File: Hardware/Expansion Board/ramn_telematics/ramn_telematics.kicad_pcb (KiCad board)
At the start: 2 copper layers, 63.3 x 33.3 mm, 43 parts, among them IC1 ESP32-S3-WROOM-1-N8, IC2 SGM2212-3.3XKC3G_TR, J1 Main RAMN Connection, J2 105164-0001, J4 105164-0001, Q1 L8050QLT1G, Q2 L8050QLT1G, U1 CP2102N-Axx-xQFN28

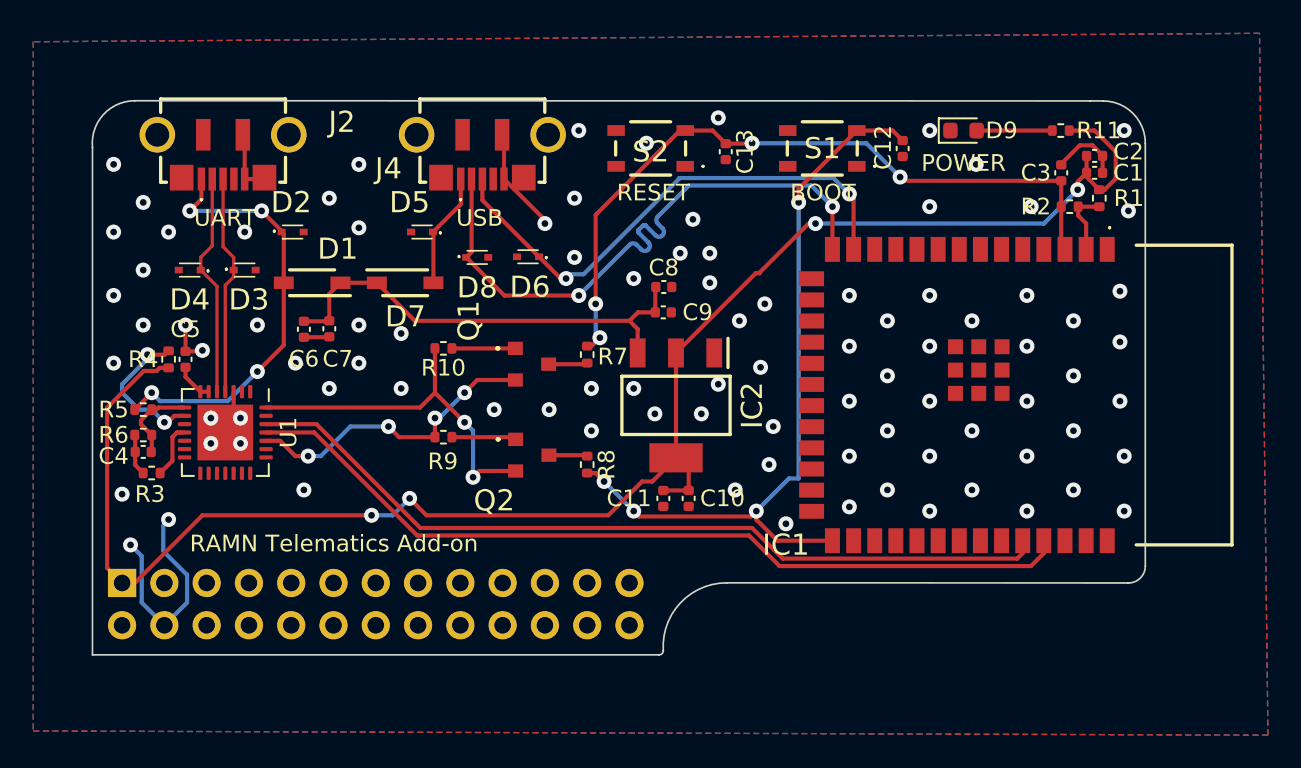
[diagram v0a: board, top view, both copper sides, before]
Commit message: More Board Revisions
Trying to update to components that are available in JLCPCB
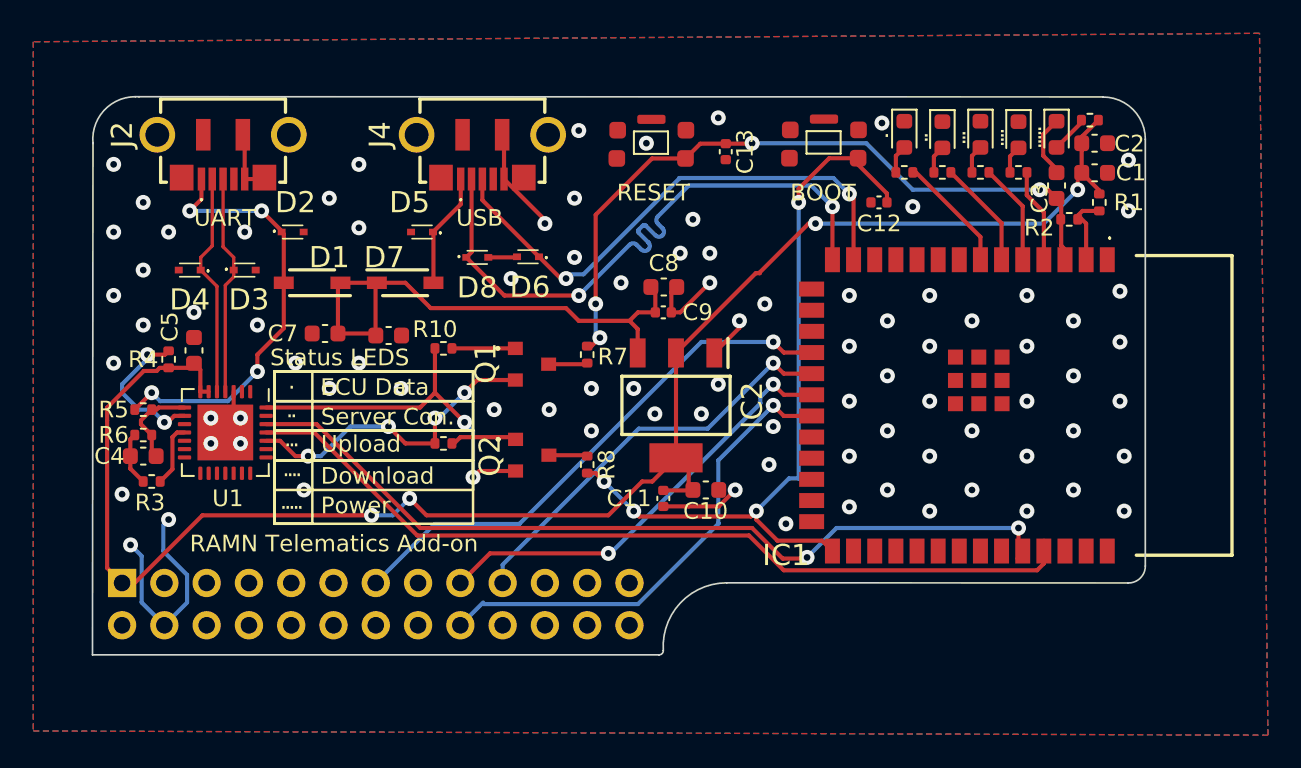
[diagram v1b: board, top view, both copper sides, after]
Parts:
- added D10: RED LED, LED_SMD:LED_0603_1608Metric, F.Cu at (184.7, 87.4)
- added D11: GRN LED, LED_SMD:LED_0603_1608Metric, F.Cu at (182.4, 87.4)
- added D12: AMB LED, LED_SMD:LED_0603_1608Metric, F.Cu at (180.1, 87.4)
- added D13: AMB LED, LED_SMD:LED_0603_1608Metric, F.Cu at (177.8, 87.4)
- added R12: 5.1K(1%), Resistor_SMD:R_0402_1005Metric, F.Cu at (184.7, 89.6)
- added R13: 5.1K(1%), Resistor_SMD:R_0402_1005Metric, F.Cu at (182.4, 89.6)
- added R14: 5.1K(1%), Resistor_SMD:R_0402_1005Metric, F.Cu at (180.1, 89.6)
- added R15: 5.1K(1%), Resistor_SMD:R_0402_1005Metric, F.Cu at (177.8, 89.6)
- C1, C10, C2, C3, C4, C5, C6, C7, C8: footprint Capacitor_SMD:C_0402_1005Metric -> Capacitor_SMD:C_0603_1608Metric
- S1, S2: value NTC013-AT1J-A160T -> KMR221GLFS; footprint SamacSys_Parts:NTC013AT1JA160T -> Library:KMR221GLFS_PUSH_SMD_SWITCH_2.8mmx1.9mm
- moved D9 5.59 mm to (186.9, 87.4), turned to -90 degrees
- moved C6 5.11 mm to (146.8, 99.4), turned to 180 degrees
- moved C12 3.54 mm to (176.3, 91.4), turned to 180 degrees
- moved R11 1.86 mm to (188.9, 86.5)
- moved C10 1.15 mm to (165.9, 108.7), turned to 0 degrees
- moved C3 0.81 mm to (186.9, 90.4)
- moved R2 0.76 mm to (187.7, 92.5)
- moved C2 0.76 mm to (189.2, 87.9)
- moved C5 0.74 mm to (135.1, 100.3)
- moved IC1 0.62 mm to (184.7, 103.6)
- moved R3 0.51 mm to (132.6, 108.2)
- moved C7 0.38 mm to (143.0, 99.3), turned to 0 degrees
- moved R9 0.38 mm to (150.1, 105.9)
- moved S1 0.33 mm to (173.0, 87.9), turned to 0 degrees
- moved S2 0.30 mm to (162.6, 87.9), turned to 0 degrees
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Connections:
- IC1 pad 18: /GPIO10 -> /CS
- IC1 pad 19: /GPIO11 -> /MOSI
- IC1 pad 20: /GPIO12 -> /SCK
- IC1 pad 21: /GPIO13 -> /MISO
- J1 pad 13: LCD_CS -> /CS
- J1 pad 17: SCK -> /SCK
- J1 pad 18: MISO -> /MISO
- J1 pad 19: MOSI -> /MOSI
- S1 pad 3: /GPIO0 -> unconnected-(S1-Pad3)
- S1 pad 4: unconnected-(S1-Pad4) -> /GPIO0
- S2 pad 3: /CHIP_PU -> unconnected-(S2-Pad3)
- S2 pad 4: unconnected-(S2-Pad4) -> /CHIP_PU
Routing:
- net /CS: track 0.00 -> 32.4 mm, vias 0 -> 1
- net /MISO: track 0.00 -> 29.1 mm, vias 0 -> 1
- net /SCK: track 0.00 -> 26.5 mm, vias 0 -> 2
- net /MOSI: track 0.00 -> 24.9 mm, vias 0 -> 1
- net GND: track 37.7 -> 47.4 mm, vias 92 -> 87
- net /GPIO7: track 0.00 -> 6.42 mm
- net /GPIO6: track 0.00 -> 5.89 mm
- net /GPIO5: track 0.00 -> 5.46 mm
- net /GPIO4: track 0.00 -> 5.06 mm
- net /VCC_5V: track 27.8 -> 32.2 mm
- net Net-(D9-A): track 4.54 -> 2.26 mm
- net /3V3_ECU: track 103.2 -> 101.4 mm
- net Net-(D13-A): track 0.00 -> 1.71 mm
- net Net-(D11-A): track 0.00 -> 1.71 mm
- net Net-(D12-A): track 0.00 -> 1.68 mm
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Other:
- board size 63.3 x 33.3 mm -> 63.2 x 33.5 mm
- board text added: "."
- board text added: "Download"
- board text added: "ECU Data"
- board text added: "Power"
- board text added: "Server Con."
- board text added: "Status LEDS"
- board text added: "Upload"
- board text removed: "POWER"
